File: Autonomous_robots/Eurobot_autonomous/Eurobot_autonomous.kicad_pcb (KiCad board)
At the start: 2 copper layers, 62.2 x 62.5 mm, 20 parts, among them J1 Conn_01x02, J2 Conn_01x03, J3 Conn_01x03, J4 Conn_01x03, M1 Motor_Servo, M2 Motor_DC, M3 Motor_DC, SW1 SW_DIP_x01, U1 dc-dc_converter, U2 DRV8870DDA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

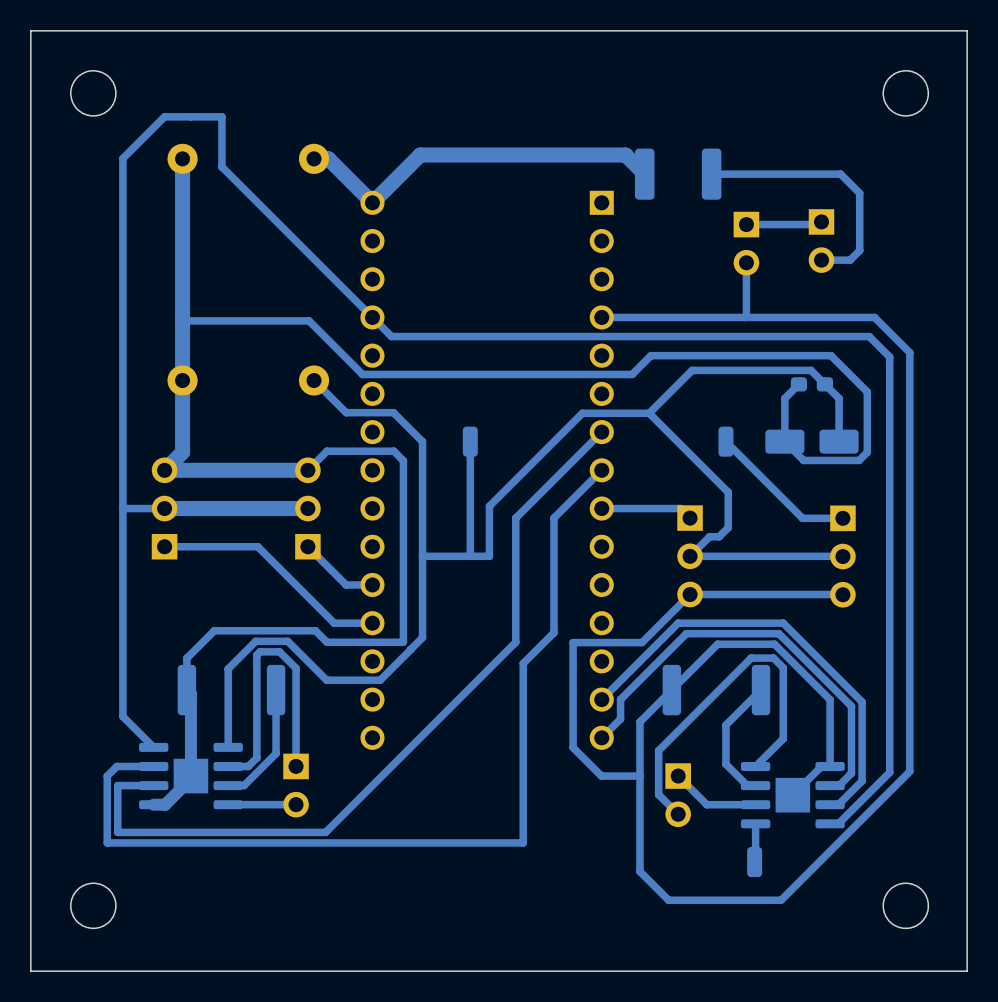
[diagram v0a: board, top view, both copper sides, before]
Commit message: 3D models of autonomous robots updated
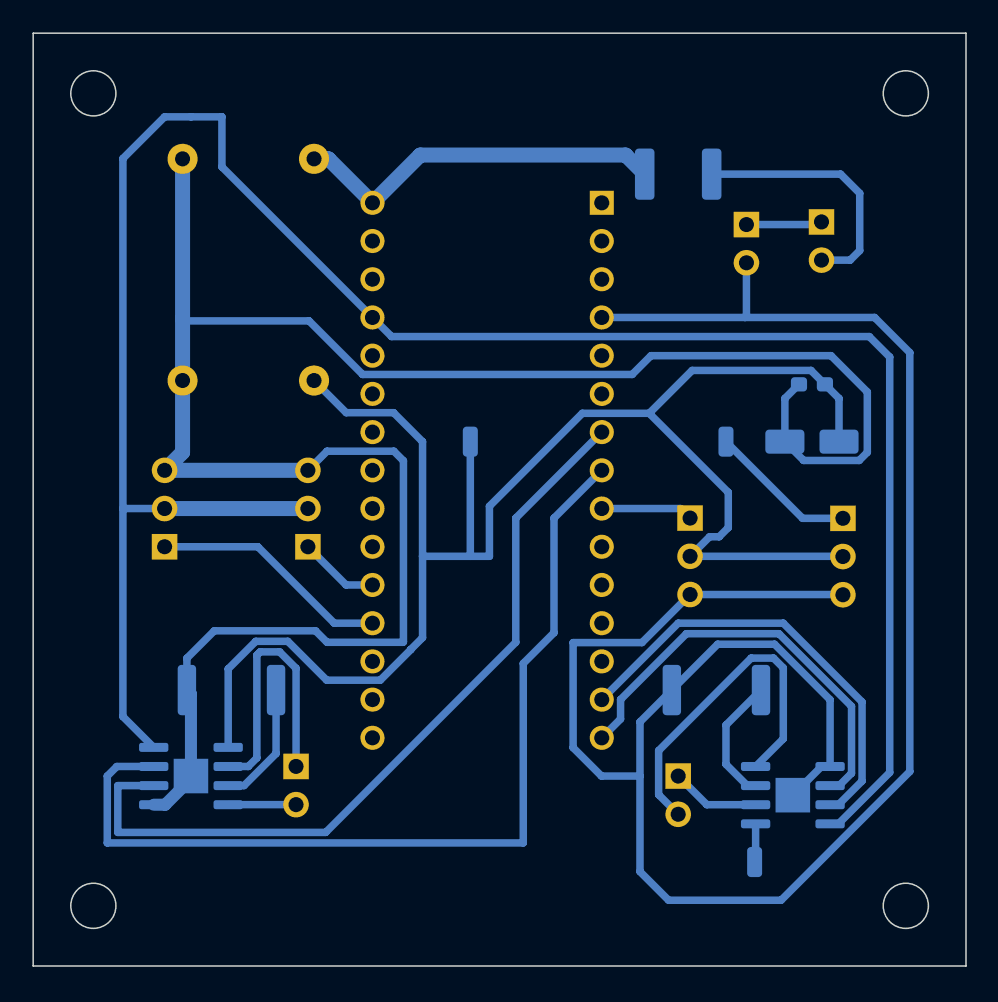
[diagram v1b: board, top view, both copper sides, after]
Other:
- board size 62.2 x 62.5 mm -> 62 x 62 mm
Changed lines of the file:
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@@
     )
   )
-  (gr_rect (start 29.845 29.845) (end 92.075 92.345) (layer "Edge.Cuts") (width 0.1) (fill none))
+  (gr_rect (start 30 30) (end 92 92) (layer "Edge.Cuts") (width 0.1) (fill none))
   (gr_circle (center 34 88) (end 35.5 88) (layer "Edge.Cuts") (width 0.1) (fill none))
   (gr_circle (center 88 34) (end 89.5 34) (layer "Edge.Cuts") (width 0.1) (fill none))

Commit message: PCB for autonomous robots updated
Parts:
- removed the REF** at (78.0, 85.1)
- added REF**: SolderWirePad_1x01_SMD_1x2mm, Connector_Wire:SolderWirePad_1x01_SMD_1x2mm, F.Cu at (71.6, 71.6)
- added REF**: SolderWirePad_1x01_SMD_1x2mm, Connector_Wire:SolderWirePad_1x01_SMD_1x2mm, F.Cu at (38.6, 42.2)
- added REF**: SolderWirePad_1x01_SMD_1x2mm, Connector_Wire:SolderWirePad_1x01_SMD_1x2mm, F.Cu at (40.0, 69.2)
- added REF**: SolderWirePad_1x01_SMD_1x2mm, Connector_Wire:SolderWirePad_1x01_SMD_1x2mm, F.Cu at (74.2, 48.8)
- moved F1 12.4 mm to (60.5, 38.6)
- moved C1 6.12 mm to (83.6, 47.5)
- moved C2 6.12 mm to (83.6, 51.3)
- moved REF** 6.12 mm to (77.9, 51.3)
- moved J1 5.80 mm to (72.7, 39.3)
- moved SW1 5.80 mm to (77.7, 39.1)
- moved J2 5.37 mm to (84.3, 56.9)
- moved M1 5.37 mm to (74.2, 56.9)
- moved M2 4.62 mm to (71.6, 83.8)
- moved U1 4.14 mm to (41.7, 45.7), turned to -90 degrees
- moved R1 3.33 mm to (78.7, 73.7)
- moved U2 1.67 mm to (80.3, 82.3), turned to 0 degrees
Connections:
- A1 pad 29: unconnected-(A1-Pad29) -> GNDD
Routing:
- net GNDD: track 281.6 -> 200.8 mm
- net Net-(M2-Pad1): track 5.93 -> 72.0 mm
- net +5V: track 146.0 -> 113.7 mm
- net Net-(A1-Pad30): track 34.9 -> 52.8 mm
- net +6V: track 114.9 -> 130.9 mm
- net Net-(A1-Pad15): track 28.4 -> 14.1 mm
- net Net-(A1-Pad14): track 29.6 -> 15.7 mm
- net Net-(M2-Pad2): track 23.2 -> 12.0 mm
- net Net-(F1-Pad2): track 17.0 -> 27.5 mm
- net Net-(R1-Pad1): track 8.45 -> 18.3 mm
- net Net-(A1-Pad7): track 53.5 -> 60.3 mm
- net Net-(A1-Pad9): track 6.13 -> 8.33 mm
- net Net-(A1-Pad8): track 62.4 -> 64.5 mm

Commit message: PCB for autonomous robots updated
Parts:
- moved M3 5.09 mm to (47.2, 83.8)
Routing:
- net Net-(A1-Pad7): track 60.3 -> 68.0 mm
- net Net-(M3-Pad1): track 18.6 -> 26.0 mm
- net Net-(A1-Pad8): track 64.5 -> 71.5 mm
- net Net-(M3-Pad2): track 5.22 -> 9.65 mm
- net +6V: track 130.9 -> 134.3 mm
- net Net-(R2-Pad1): track 8.29 -> 9.13 mm

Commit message: wip
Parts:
- removed the REF** at (71.6, 71.6)
- removed the REF** at (38.6, 42.2)
- removed the REF** at (40.0, 69.2)
- removed the REF** at (74.2, 48.8)
- removed the REF** at (59.1, 57.1)
- added REF**: SolderWirePad_SMD_2x2mm, Eurobot_2025:SolderWirePad_SMD_2x2mm, F.Cu at (74.2, 48.8)
- added REF**: SolderWirePad_SMD_3x3mm, Eurobot_2025:SolderWirePad_SMD_3x3mm, F.Cu at (38.6, 43.2)
- added REF**: SolderWirePad_SMD_3x3mm, Eurobot_2025:SolderWirePad_SMD_3x3mm, F.Cu at (58.9, 53.8)
- added REF**: SolderWirePad_SMD_2x2mm, Eurobot_2025:SolderWirePad_SMD_2x2mm, F.Cu at (40.1, 68.6)
- added REF**: SolderWirePad_SMD_2x4mm, Eurobot_2025:SolderWirePad_SMD_2x4mm, F.Cu at (77.7, 84.8)
- moved M2 5.90 mm to (74.2, 78.5), turned to 0 degrees
- moved M3 5.87 mm to (47.8, 78.0)
- moved U2 3.00 mm to (81.9, 79.8), turned to 180 degrees
- moved R1 2.59 mm to (81.3, 73.2), turned to 0 degrees
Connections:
- A1 pad 14: Net-(A1-Pad14) -> Net-(U2-Pad2)
- A1 pad 15: Net-(A1-Pad15) -> Net-(U2-Pad3)
- U2 pad 2: Net-(A1-Pad15) -> Net-(U2-Pad2)
- U2 pad 3: Net-(A1-Pad14) -> Net-(U2-Pad3)
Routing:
- net Net-(M2-Pad1): track 72.0 -> 6.00 mm
- net Net-(U2-Pad2): track 0.00 -> 53.4 mm
- net +6V: track 134.3 -> 181.5 mm
- net Net-(U2-Pad3): track 0.00 -> 35.9 mm
- net Net-(A1-Pad14): track 15.7 -> 0.00 mm
- net Net-(A1-Pad15): track 14.1 -> 0.00 mm
- net Net-(R1-Pad1): track 18.3 -> 7.16 mm
- net Net-(M2-Pad2): track 12.0 -> 19.2 mm
- net +5V: track 113.7 -> 107.3 mm
- net Net-(M3-Pad1): track 26.0 -> 21.0 mm
- net Net-(A1-Pad7): track 68.0 -> 64.1 mm
- net Net-(M3-Pad2): track 9.65 -> 5.82 mm
- net GNDD: track 201.1 -> 197.9 mm
- net Net-(A1-Pad8): track 71.5 -> 68.7 mm
